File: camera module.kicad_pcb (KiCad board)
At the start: 2 copper layers, 100.1 x 100.2 mm, 156 parts, among them J1 Conn_01x02, J10 Conn_01x04, J11 Conn_01x05, J12 Conn_01x06, J13 Conn_01x02, J15 Conn_02x30_Odd_Even, J17 USB_B_Micro, J18 Conn_01x03, J2 USB_OTG, J3 Conn_01x15, J4 Conn_02x15_Counter_Clockwise, J5 HDMI, J6 Conn_01x15, J7 Conn_01x02, J8 HDMI, J9 HDMI, Q1 EM6K34T2CR, Q10 DMG2305UX, Q11 DMMT5401-7-F, Q12 DMG2305UX, Q2 Q_NMOS_GSD, Q3 Q_NMOS_GSD, Q4 Q_NMOS_GSD, Q5 Q_NMOS_GSD, Q6 Q_NMOS_GSD, Q7 DMMT5401-7-F, Q8 DMG2305UX, Q9 DMMT5401-7-F, SW1 SW_SPST, U1 TPS563208, U10 FSUSB42UMX, U11 USB_A, U2 PAM2306AYPKE, U3 LTC3406ES5-1.2, U4 TS3DDR3812RUAR, U5 TLV70228_SOT23-5, U6 XC6222B181MR-G, U7 LSM6DS3, U8 HDMIULC6-4SC6, U9 AP2331W, Y1 SIT8008AI-73-XXS-33.333333E

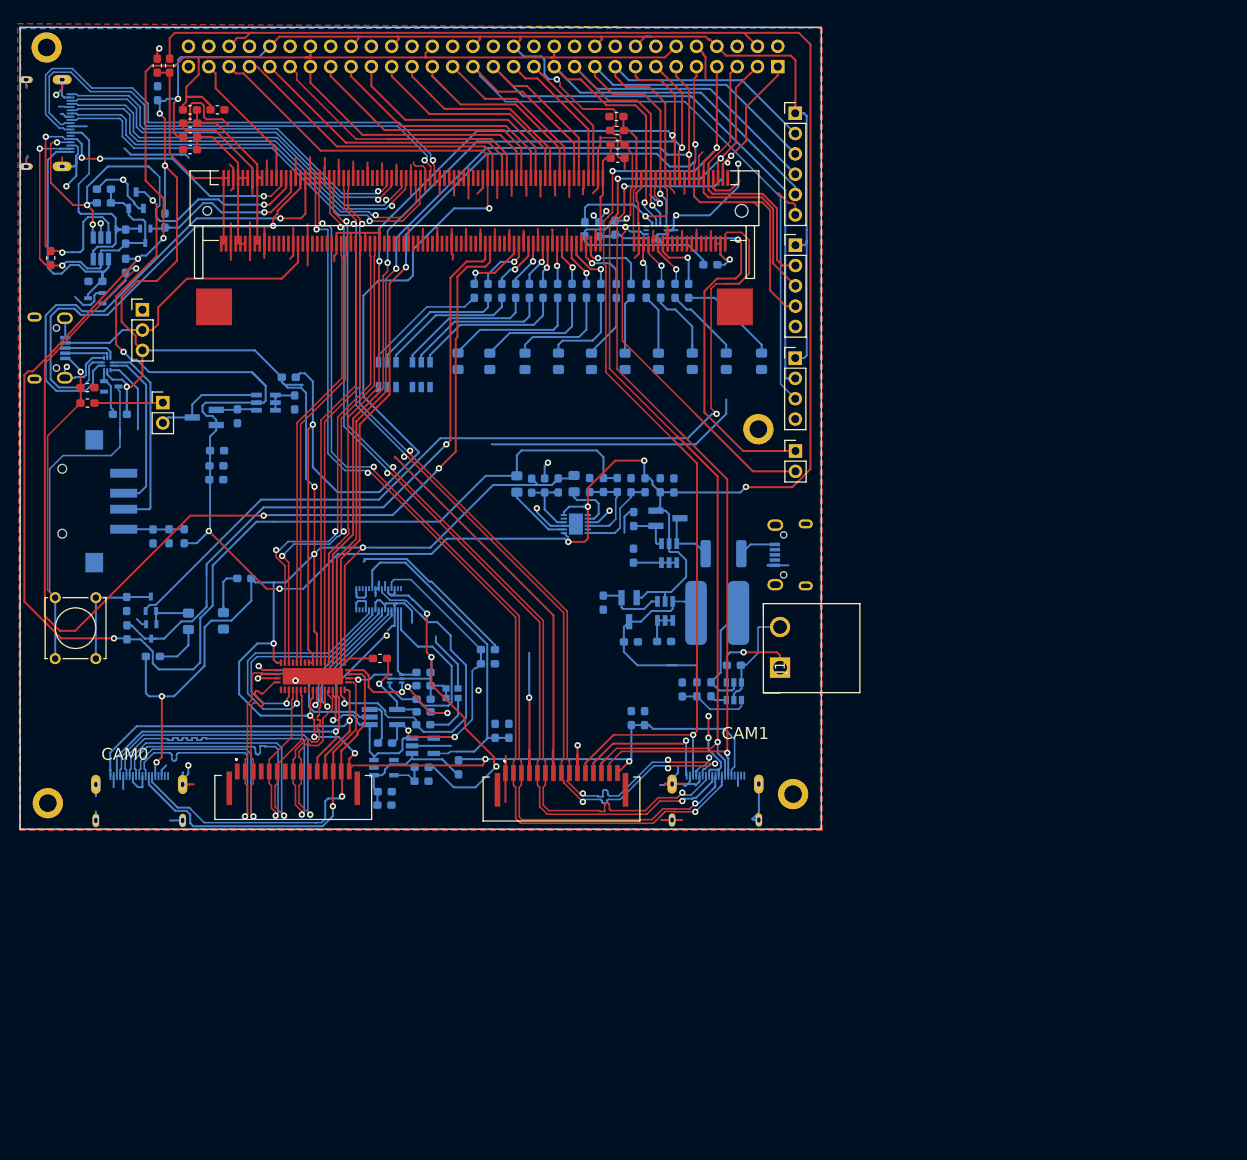
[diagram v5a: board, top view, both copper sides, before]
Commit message: Uploaded the start of V1
libraries are now compliant with license, and schematic has been slightly changed to be cheaper, MOSFET footprints also fixed
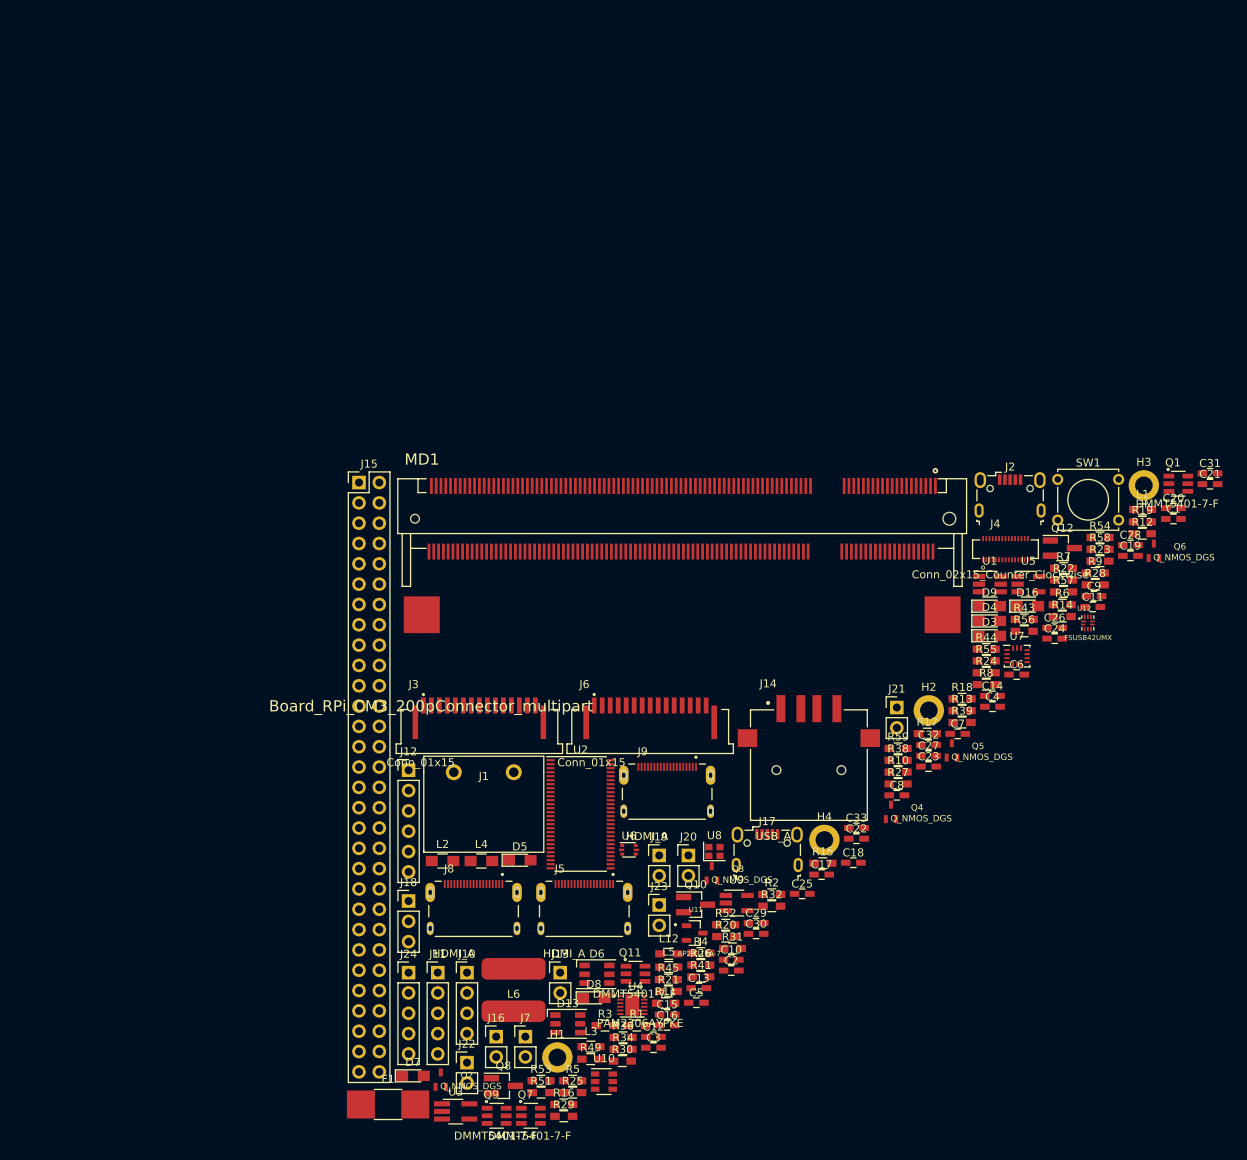
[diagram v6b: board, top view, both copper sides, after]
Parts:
- removed D10, D11, D12, D14, D15: LED, LED_SMD:LED_0805_2012Metric_Pad1.15x1.40mm_HandSolder
- removed R33, R35, R37, R40, R42: 470R, Resistor_SMD:R_0603_1608Metric_Pad1.05x0.95mm_HandSolder
- removed Y1: SIT8008AI-73-XXS-33.333333E, SIT8008AI-73-XXS-33.333333E:2.0X1.6X0.75MM
- added J14: USB_A, USB_A connector:TE_1-292303-6, F.Cu at (146.2, 128.9)
- added J16: Conn_01x02, Socket_Strips:Socket_Strip_Straight_1x02_Pitch2.54mm, F.Cu at (107.1, 162.2)
- added J19: Conn_01x02, Socket_Strips:Socket_Strip_Straight_1x02_Pitch2.54mm, F.Cu at (127.4, 139.5)
- added J20: Conn_01x02, Socket_Strips:Socket_Strip_Straight_1x02_Pitch2.54mm, F.Cu at (131.1, 139.5)
- added J21: Conn_01x02, Socket_Strips:Socket_Strip_Straight_1x02_Pitch2.54mm, F.Cu at (157.1, 121.0)
- added J22: Conn_01x02, Socket_Strips:Socket_Strip_Straight_1x02_Pitch2.54mm, F.Cu at (103.4, 165.4)
- added J23: Conn_01x02, Socket_Strips:Socket_Strip_Straight_1x02_Pitch2.54mm, F.Cu at (127.4, 145.7)
- added J24: Conn_01x05, Pin_Headers:Pin_Header_Straight_1x05_Pitch2.54mm, F.Cu at (96.1, 154.2)
- added U12: FSUSB42UMX, FSUSB42UMX:IC_FSUSB42UMX, F.Cu at (181.0, 110.5)
- C1, C10, C11, C13, C15, C16, C17, C18, C19, C2, C24, C25, C26, C27, C28, C29, C3, C30, C31, C32, C33, C4, C5, C6, C7, C8, C9: footprint Capacitor_SMD:C_0603_1608Metric_Pad1.05x0.95mm_HandSolder -> Capacitors_SMD:C_0603_HandSoldering; moved to F.Cu
- C12, C14, C20, C21, C22, C23: footprint Capacitor_SMD:C_0603_1608Metric_Pad1.05x0.95mm_HandSolder -> Capacitors_SMD:C_0603_HandSoldering
- D13, D6: footprint LED_SMD:LED_RGB_PLCC-6 -> LEDs:LED_RGB_PLCC-6; moved to F.Cu
- D16, D3, D4, D5, D7, D8, D9: footprint LED_SMD:LED_0805_2012Metric_Pad1.15x1.40mm_HandSolder -> LEDs:LED_0805_HandSoldering; moved to F.Cu
- F1: footprint Fuse:Fuse_1812_4532Metric_Pad1.30x3.40mm_HandSolder -> Inductors_SMD:L_1812_HandSoldering; moved to F.Cu
- H1, H2, H3, H4: footprint MountingHole:MountingHole_2.2mm_M2_DIN965_Pad -> Mounting_Holes:MountingHole_2.2mm_M2_DIN965_Pad
- J1: footprint 8971266:SHDR3W150P0X508_1X3_1640X1210X830P -> CAMCONs:7.5mm Camcon
- J10: footprint Connector_PinHeader_2.54mm:PinHeader_1x04_P2.54mm_Vertical -> Pin_Headers:Pin_Header_Straight_1x04_Pitch2.54mm
- J11: footprint Connector_PinHeader_2.54mm:PinHeader_1x05_P2.54mm_Vertical -> Pin_Headers:Pin_Header_Straight_1x05_Pitch2.54mm
- J12: footprint Connector_PinHeader_2.54mm:PinHeader_1x06_P2.54mm_Vertical -> Pin_Headers:Pin_Header_Straight_1x06_Pitch2.54mm
- J13, J7: footprint Connector_PinHeader_2.54mm:PinHeader_1x02_P2.54mm_Vertical -> Pin_Headers:Pin_Header_Straight_1x02_Pitch2.54mm
- J15: footprint Connector_PinHeader_2.54mm:PinHeader_2x30_P2.54mm_Vertical -> Pin_Headers:Pin_Header_Straight_2x30_Pitch2.54mm; moved to F.Cu
- J17, J2: footprint Connector_USB:USB_Micro-B_Wuerth_629105150521 -> Connectors_USB:USB_Micro-B_Wuerth-629105150521; moved to F.Cu
- J18: footprint Connector_PinHeader_2.54mm:PinHeader_1x03_P2.54mm_Vertical -> Pin_Headers:Pin_Header_Straight_1x03_Pitch2.54mm
- J3, J6: footprint SFW15R-2STE1LF:SFW15R2STE1LF -> SFW15R-1STE1LF:AMPHENOL_SFW15R-1STE1LF
- J4, Q11, Q7, Q9: moved to F.Cu
- J5, J8, J9: value HDMI -> HDMI_A; footprint 685119136923:WURTH_685119136923 -> HDMI connector:WURTH_685119136923; moved to F.Cu
- L1: footprint Inductor_SMD:L_0603_1608Metric_Pad1.05x0.95mm_HandSolder -> Inductors_SMD:L_0603_HandSoldering
- L12, L3, L5: footprint Inductor_SMD:L_0603_1608Metric_Pad1.05x0.95mm_HandSolder -> Inductors_SMD:L_0603_HandSoldering; moved to F.Cu
- L2, L4: footprint Inductor_SMD:L_0805_2012Metric_Pad1.15x1.40mm_HandSolder -> Inductors_SMD:L_0805_HandSoldering; moved to F.Cu
- L6: footprint Inductor_SMD_local:SDR0805-3R3ML-footprint -> SDR0805:SDR0805; moved to F.Cu
- Q1: value EM6K34T2CR -> DMMT5401-7-F; footprint Package_TO_SOT_SMD:SOT-563 -> DMMT5401-7-F:SOT95P285X140-6N; moved to F.Cu
- Q10, Q12, Q8: footprint Package_TO_SOT_SMD:SOT-23_Handsoldering -> TO_SOT_Packages_SMD:SOT-23_Handsoldering; moved to F.Cu
- Q2, Q3, Q4, Q5, Q6: value Q_NMOS_GSD -> Q_NMOS_DGS; moved to F.Cu
- R1, R10, R11, R12, R13, R16, R19, R2, R21, R22, R23, R24, R25, R26, R27, R28, R29, R3, R30, R31, R32, R34, R36, R38, R39, R4, R41, R43, R44, R45, R5, R52, R53, R54, R55, R56, R57, R58, R59, R7, R8, R9: footprint Resistor_SMD:R_0603_1608Metric_Pad1.05x0.95mm_HandSolder -> Resistors_SMD:R_0603_HandSoldering; moved to F.Cu
- R14, R15, R17, R18, R20, R49, R51, R6: footprint Resistor_SMD:R_0603_1608Metric_Pad1.05x0.95mm_HandSolder -> Resistors_SMD:R_0603_HandSoldering
- SW1: footprint Button_Switch_THT:SW_Tactile_Straight_KSL0Axx1LFTR -> Buttons_Switches_THT:SW_Tactile_Straight_KSL0Axx1LFTR
- U1: footprint Package_TO_SOT_SMD:SOT-23-6 -> TO_SOT_Packages_SMD:SOT-23-6_Handsoldering; moved to F.Cu
- U10: value FSUSB42UMX -> HDMIULC6-4SC6; footprint FSUSB42UMX:IC_FSUSB42UMX -> TO_SOT_Packages_SMD:SOT-23-6; moved to F.Cu
- U11: value USB_A -> AP2331SA-7; footprint 1-292303-6:TE_1-292303-6 -> AP2331SA-7:SOT91P240X120-3N; moved to F.Cu
- U2: value PAM2306AYPKE -> FST16233MTDX; footprint PAM2306AYPKE:SON45P300X300X80-13N -> Housings_SSOP:TSSOP-56_6.1x14mm_Pitch0.5mm; moved to F.Cu
- U3: footprint Package_TO_SOT_SMD:TSOT-23-5_HandSoldering -> TO_SOT_Packages_SMD:TSOT-23-5_HandSoldering; moved to F.Cu
- U4: value TS3DDR3812RUAR -> PAM2306AYPKE; footprint TS3DDR3812RUAR:QFN50P350X900X80-43N -> PAM2306AYPKE:SON45P300X300X80-13N
- U5: footprint Package_TO_SOT_SMD:SOT-23-5_HandSoldering -> TO_SOT_Packages_SMD:SOT-23-5_HandSoldering; moved to F.Cu
- U6: value XC6222B181MR-G -> EM6K34T2CR; footprint SOT95P280X130-5N:SOT95P280X130-5N -> TO_SOT_Packages_SMD:SOT-666; moved to F.Cu
- U7: footprint Package_LGA:Bosch_LGA-14_3x2.5mm_P0.5mm -> Housings_LGA:Bosch_LGA-14_3x2.5mm_Pitch0.5mm; moved to F.Cu
- U8: value HDMIULC6-4SC6 -> SIT8008AI-73-XXS-33.333333E; footprint Package_TO_SOT_SMD:SOT-23-6_Handsoldering -> Crystals:Crystal_SMD_2016-4pin_2.0x1.6mm; moved to F.Cu
- U9: value AP2331W -> XC6222B181MR-G; footprint AP2331SA-7:SOT91P240X120-3N -> TO_SOT_Packages_SMD:SOT-23-5_HandSoldering; moved to F.Cu
- moved H1 141.5 mm to (114.7, 164.8)
- moved R19 135.8 mm to (187.8, 97.8), turned to 0 degrees
- moved Q6 131.9 mm to (189.3, 101.5), turned to 0 degrees
- moved C22 130.3 mm to (152.1, 137.4), turned to 0 degrees
- moved C30 129.0 mm to (139.6, 149.3), turned to 0 degrees
- moved C12 128.1 mm to (126.7, 162.2), turned to 0 degrees
- moved SW1 127.3 mm to (177.3, 92.5), turned to 0 degrees
- moved R22 126.6 mm to (178.0, 105.1), turned to 0 degrees
- moved R17 126.3 mm to (161.0, 124.3), turned to 0 degrees
- moved R6 125.4 mm to (177.8, 108.2), turned to 0 degrees
- moved C27 125.1 mm to (161.1, 127.1), turned to 0 degrees
- moved C28 122.2 mm to (186.3, 100.7), turned to 0 degrees
- moved C14 121.5 mm to (169.1, 119.6)
- moved C23 120.3 mm to (161.1, 128.4), turned to 0 degrees
- moved C1 119.9 mm to (191.7, 97.5)
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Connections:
- C26 pad 1: 5V -> GND
- C26 pad 2: GND -> 5V
- J15 pad 55: CAM0_offboard_n -> (no net)
- J15 pad 59: Net-(J15-Pad59) -> (no net)
- J2 pad 2: Net-(J2-Pad2) -> (no net)
- J2 pad 3: Net-(J2-Pad3) -> (no net)
- J2 pad 4: Net-(J2-Pad4) -> (no net)
- J4 pad 13: Net-(J4-Pad13) -> (no net)
- J4 pad 14: Net-(J4-Pad14) -> (no net)
- J4 pad 17: Net-(J4-Pad17) -> (no net)
- J4 pad 18: Net-(J4-Pad18) -> (no net)
- J4 pad 20: Net-(J4-Pad20) -> (no net)
- J4 pad 29: Net-(J4-Pad29) -> (no net)
- J4 pad 30: Net-(J4-Pad30) -> (no net)
- J5 pad 16: Net-(J5-Pad16) -> (no net)
- J5 pad 18: Net-(J5-Pad18) -> (no net)
- J5 pad 19: Net-(J5-Pad19) -> (no net)
- J8 pad 14: Net-(J8-Pad14) -> (no net)
- J9 pad 16: Net-(J9-Pad16) -> (no net)
- J9 pad 18: Net-(J9-Pad18) -> (no net)
- J9 pad 19: Net-(J9-Pad19) -> (no net)
- MD1 pad 10: Net-(MD1-Pad10) -> (no net)
- MD1 pad 100: Net-(MD1-Pad100) -> (no net)
- MD1 pad 101: Net-(MD1-Pad101) -> (no net)
- MD1 pad 102: Net-(MD1-Pad102) -> (no net)
- MD1 pad 105: Net-(MD1-Pad105) -> (no net)
- MD1 pad 106: Net-(MD1-Pad106) -> (no net)
- MD1 pad 107: Net-(MD1-Pad107) -> (no net)
- MD1 pad 108: Net-(MD1-Pad108) -> (no net)
- MD1 pad 11: CAM1_IO0 -> (no net)
- MD1 pad 112: Net-(MD1-Pad112) -> (no net)
- MD1 pad 114: Net-(MD1-Pad114) -> (no net)
- MD1 pad 118: Net-(MD1-Pad118) -> (no net)
- MD1 pad 12: Net-(MD1-Pad12) -> (no net)
- MD1 pad 120: Net-(MD1-Pad120) -> (no net)
- MD1 pad 124: Net-(MD1-Pad124) -> (no net)
- MD1 pad 126: Net-(MD1-Pad126) -> (no net)
- MD1 pad 128: Net-(MD1-Pad128) -> (no net)
- MD1 pad 130: Net-(MD1-Pad130) -> (no net)
- MD1 pad 132: Net-(MD1-Pad132) -> (no net)
- MD1 pad 135: Net-(MD1-Pad135) -> (no net)
- MD1 pad 137: Net-(MD1-Pad137) -> (no net)
- MD1 pad 141: Net-(MD1-Pad141) -> (no net)
- MD1 pad 143: Net-(MD1-Pad143) -> (no net)
- MD1 pad 15: CD0_SDA -> (no net)
- MD1 pad 154: Net-(MD1-Pad154) -> (no net)
- MD1 pad 156: Net-(MD1-Pad156) -> (no net)
- MD1 pad 158: Net-(MD1-Pad158) -> (no net)
- MD1 pad 16: Net-(MD1-Pad16) -> (no net)
- MD1 pad 160: Net-(MD1-Pad160) -> (no net)
- MD1 pad 162: Net-(MD1-Pad162) -> (no net)
- MD1 pad 166: TVDAC -> (no net)
- MD1 pad 172: Net-(MD1-Pad172) -> (no net)
- MD1 pad 174: Net-(MD1-Pad174) -> (no net)
- MD1 pad 176: Net-(MD1-Pad176) -> (no net)
- MD1 pad 178: Net-(MD1-Pad178) -> (no net)
- MD1 pad 179: Net-(MD1-Pad179) -> (no net)
- MD1 pad 18: Net-(MD1-Pad18) -> (no net)
- MD1 pad 180: Net-(MD1-Pad180) -> (no net)
- MD1 pad 22: Net-(MD1-Pad22) -> (no net)
- MD1 pad 24: Net-(MD1-Pad24) -> (no net)
- MD1 pad 48: GPIO33 -> (no net)
- MD1 pad 52: GPIO34 -> (no net)
- MD1 pad 54: GPIO35 -> (no net)
- MD1 pad 58: GPIO36 -> (no net)
- MD1 pad 60: GPIO37 -> (no net)
- MD1 pad 82: Net-(MD1-Pad82) -> (no net)
- MD1 pad 84: Net-(MD1-Pad84) -> (no net)
- MD1 pad 89: CAM0_offboard_n -> CAM0_onboard_n
- MD1 pad 9: CAM1_CLK -> (no net)
- MD1 pad 93: Net-(MD1-Pad93) -> (no net)
- MD1 pad 94: Net-(MD1-Pad94) -> (no net)
- MD1 pad 95: Net-(MD1-Pad95) -> (no net)
- MD1 pad 96: Net-(MD1-Pad96) -> (no net)
- MD1 pad 99: Net-(MD1-Pad99) -> (no net)
- Q1 pad 1: Net-(J4-Pad2) -> Net-(Q1-Pad1)
- Q1 pad 2: CAM_1V8 -> Net-(Q1-Pad1)
- Q1 pad 3: CD0_onboard_SDA -> Net-(Q1-Pad1)
- Q1 pad 4: Net-(J4-Pad1) -> Net-(Q1-Pad4)
- Q1 pad 5: CAM_1V8 -> 5V
- Q1 pad 6: CD0_onboard_SCL -> Net-(F1-Pad1)
- Q11 pad 2: Net-(Q11-Pad1) -> Net-(Q11-Pad2)
- Q11 pad 3: Net-(Q11-Pad1) -> (no net)
- Q11 pad 4: Net-(Q11-Pad4) -> (no net)
- Q11 pad 5: 5V -> (no net)
- Q11 pad 6: Net-(J13-Pad2) -> 5V
- Q12 pad 1: Net-(Q11-Pad4) -> Net-(Q11-Pad1)
- Q2 pad 1: H5V -> HDMI_CEC
- Q2 pad 2: Net-(J8-Pad13) -> H5V
- Q2 pad 3: HDMI_CEC -> Net-(J8-Pad13)
- Q3 pad 1: HDMI_HPD -> HDMI_HPD_N_1V8
- Q3 pad 2: GND -> HDMI_HPD
- Q3 pad 3: HDMI_HPD_N_1V8 -> GND
- Q4 pad 1: Net-(Q4-Pad1) -> EMMC_DISABLE_N
- Q4 pad 2: Net-(D16-Pad1) -> Net-(Q4-Pad2)
- Q4 pad 3: EMMC_DISABLE_N -> Net-(D16-Pad1)
- Q5 pad 1: EMMC_EN_N_1V8 -> Net-(D16-Pad1)
- Q5 pad 2: GND -> EMMC_EN_N_1V8
- Q5 pad 3: Net-(D16-Pad1) -> GND
- Q6 pad 1: VBUSB -> Net-(Q6-Pad1)
- Q6 pad 2: GND -> VBUSB
- Q6 pad 3: Net-(Q6-Pad3) -> GND
- Q7 pad 4: Net-(Q7-Pad4) -> Net-(Q10-Pad1)
- Q7 pad 6: Net-(F1-Pad1) -> Net-(C33-Pad1)
- Q8 pad 1: Net-(Q7-Pad4) -> Net-(Q1-Pad4)
- Q9 pad 1: Net-(Q9-Pad1) -> Net-(Q11-Pad2)
- Q9 pad 2: Net-(Q9-Pad1) -> Net-(Q11-Pad2)
- Q9 pad 3: Net-(Q9-Pad1) -> (no net)
- Q9 pad 4: Net-(Q10-Pad1) -> (no net)
- Q9 pad 5: 5V -> (no net)
- Q9 pad 6: Net-(C33-Pad1) -> Net-(J13-Pad2)
- R3 pad 2: CAM0_offboard_n -> CAM0_onboard_n
- R38 pad 1: Net-(Q4-Pad1) -> Net-(Q4-Pad2)
- R45 pad 1: Net-(Q6-Pad3) -> 3V3
- R45 pad 2: 3V3 -> Net-(Q6-Pad1)
- R52 pad 1: Net-(Q7-Pad1) -> Net-(Q1-Pad1)
- R53 pad 1: Net-(Q7-Pad4) -> Net-(Q1-Pad4)
- R56 pad 1: Net-(Q9-Pad1) -> Net-(Q7-Pad1)
- R58 pad 1: Net-(Q11-Pad1) -> Net-(Q11-Pad2)
- R59 pad 1: Net-(Q11-Pad4) -> Net-(Q11-Pad1)
- SW1 pad 2: Net-(Q4-Pad1) -> Net-(Q4-Pad2)
- U10 pad 1: USB_DP -> HDMI_SDA
- U10 pad 2: USB_DM -> GND
- U10 pad 3: GND -> HDMI_SCL
- U10 pad 4: /HSD1- -> HDMI_HPD
- U10 pad 5: /HSD1+ -> H5V
- U10 pad 6: /HSD2- -> Net-(J8-Pad13)
- U11 pad 1: VBUSA -> GND
- U11 pad 2: /HSD2- -> H5V
- U11 pad 3: /HSD2+ -> 5V
- U2 pad 1: 5V -> CAM0_DP0
- U2 pad 10: Net-(C8-Pad2) -> CAM0_DN1
- U2 pad 11: (no net) -> CAM0_onboard_CP
- U2 pad 12: Net-(C3-Pad1) -> CAM0_offboard_CP
- U2 pad 2: Net-(L2-Pad1) -> CD0_onboard_SCL
- U2 pad 3: GND -> CD0_offboard_SCL
- U2 pad 4: Net-(C9-Pad2) -> CAM0_DN0
- U2 pad 5: (no net) -> CAM0_onboard_IO0
- U2 pad 6: 5V -> CAM0_offboard_IO0
- U2 pad 7: 5V -> CAM0_DP1
- U2 pad 8: Net-(L4-Pad1) -> CAM0_onboard_CN
- U2 pad 9: GND -> CAM0_offboard_CN
- U4 pad 1: 3V3 -> 5V
- U4 pad 10: CAM0_offboard_n -> Net-(C8-Pad2)
- U4 pad 11: Net-(U4-Pad11) -> (no net)
- U4 pad 12: CAM0_DP1 -> Net-(C3-Pad1)
- U4 pad 13: CAM0_DN1 -> GND
- U4 pad 2: CD0_SDA -> Net-(L2-Pad1)
- U4 pad 3: CD0_SCL -> GND
- U4 pad 4: CAM0_CK -> Net-(C9-Pad2)
- U4 pad 5: CAM0_IO0 -> (no net)
- U4 pad 6: CAM0_CP -> 5V
- U4 pad 7: CAM0_CN -> 5V
- U4 pad 8: 3V3 -> Net-(L4-Pad1)
- U4 pad 9: CAM0_offboard_n -> GND
- U5 pad 4: Net-(U5-Pad4) -> (no net)
- U6 pad 1: 3V3F1 -> Net-(J4-Pad2)
- U6 pad 2: GND -> CAM_1V8
- U6 pad 3: CAM0_onboard_IO0 -> CD0_onboard_SCL
- U6 pad 4: Net-(U6-Pad4) -> Net-(J4-Pad1)
- U6 pad 5: Net-(C16-Pad1) -> CAM_1V8
- U7 pad 10: Net-(U7-Pad10) -> (no net)
- U7 pad 11: Net-(U7-Pad11) -> (no net)
- U8 pad 1: HDMI_SDA -> CAM_1V8
- U8 pad 3: HDMI_SCL -> Net-(R13-Pad2)
- U8 pad 4: HDMI_HPD -> CAM_1V8
- U9 pad 1: GND -> 3V3F1
- U9 pad 2: H5V -> GND
- U9 pad 3: 5V -> CAM0_onboard_IO0
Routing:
- net GND: track 609.9 -> 0.00 mm, vias 25 -> 0
- net 3V3: track 538.4 -> 0.00 mm, vias 17 -> 0
- net 5V: track 340.9 -> 0.00 mm, vias 8 -> 0
- net 1V8: track 264.3 -> 0.00 mm, vias 3 -> 0
- net CAM1_IO0: track 149.8 -> 0.00 mm, vias 3 -> 0
- net CAM0_offboard_n: track 149.1 -> 0.00 mm, vias 2 -> 0
- net HDMI_HPD_N_1V8: track 145.2 -> 0.00 mm, vias 3 -> 0
- net CD0_SDA: track 142.0 -> 0.00 mm, vias 2 -> 0
- net CD1_SCL: track 130.5 -> 0.00 mm, vias 3 -> 0
- net CD1_SDA: track 130.3 -> 0.00 mm, vias 3 -> 0
- net CAM1_DN0: track 123.2 -> 0.00 mm, vias 3 -> 0
- net CAM0_IO0: track 122.7 -> 0.00 mm, vias 2 -> 0
- net CAM1_DP0: track 120.8 -> 0.00 mm, vias 3 -> 0
- net CAM1_DP1: track 114.7 -> 0.00 mm, vias 3 -> 0
- net CAM1_DN1: track 114.6 -> 0.00 mm, vias 3 -> 0
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- removed copper zone on B.Cu, net GND
- removed copper zone on F.Cu, net GND
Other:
- board size 100.1 x 100.2 mm -> 11.5 x 5.7 mm
- net class Default: clearance 0.125 -> 0.2
- rule pad_to_mask_clearance: 0.051 -> 0
- rule trace_clearance: 0.125 -> 0.2
- rule trace_min: 0 -> 0.2
- rule via_min_size: 0.2 -> 0.4
- board text removed: "12 CLK MOSI MISO CS"
- board text removed: "12V in"
- board text removed: "19 18 17 16 RX TX 13"
- board text removed: "26 25 24 23 22 21 20"
- board text removed: "28"
- board text removed: "29"
- board text removed: "30"
- board text removed: "31"
- board text removed: "32"
- board text removed: "33"
- board text removed: "34"
- board text removed: "35"
- board text removed: "36"
- board text removed: "37"
- board text removed: "38 39 40"
- board text removed: "3V3"
- board text removed: "41 42 43"
- board text removed: "5V in"
- board text removed: "Boot from USB"
- board text removed: "CAM0"
- board text removed: "CAM0_CK"
- board text removed: "CAM0_IO0"
- board text removed: "CAM1"
- board text removed: "CAM1_CLK"
- board text removed: "CAM1_IO0"
- board text removed: "CD0_SCL"
- board text removed: "CD0_SDA"
- board text removed: "CD1_SCL"
- board text removed: "CD1_SDA"
- board text removed: "Cam_offboard_n"
- board text removed: "GND"
- board text removed: "GND CLK MOSI MISO CS 3V3"
- board text removed: "GND RX TX 3V3"
- board text removed: "GND SDA IO0 CLK 3V3"
- board text removed: "HDMI_OUT"
- board text removed: "NC RUN"
- board text removed: "Power over USB slave"
- board text removed: "USB OTGID"
- board text removed: "USB_host"
- board text removed: "USB_slave"
